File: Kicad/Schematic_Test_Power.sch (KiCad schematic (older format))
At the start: 17 parts, among them J201 USB_B_Micro, J202 Conn_02x01 BATTERY, SW201 SW_DIP_x01, U201 STBC08, U202 AP22811BW5, U203 TLV75528PDBV

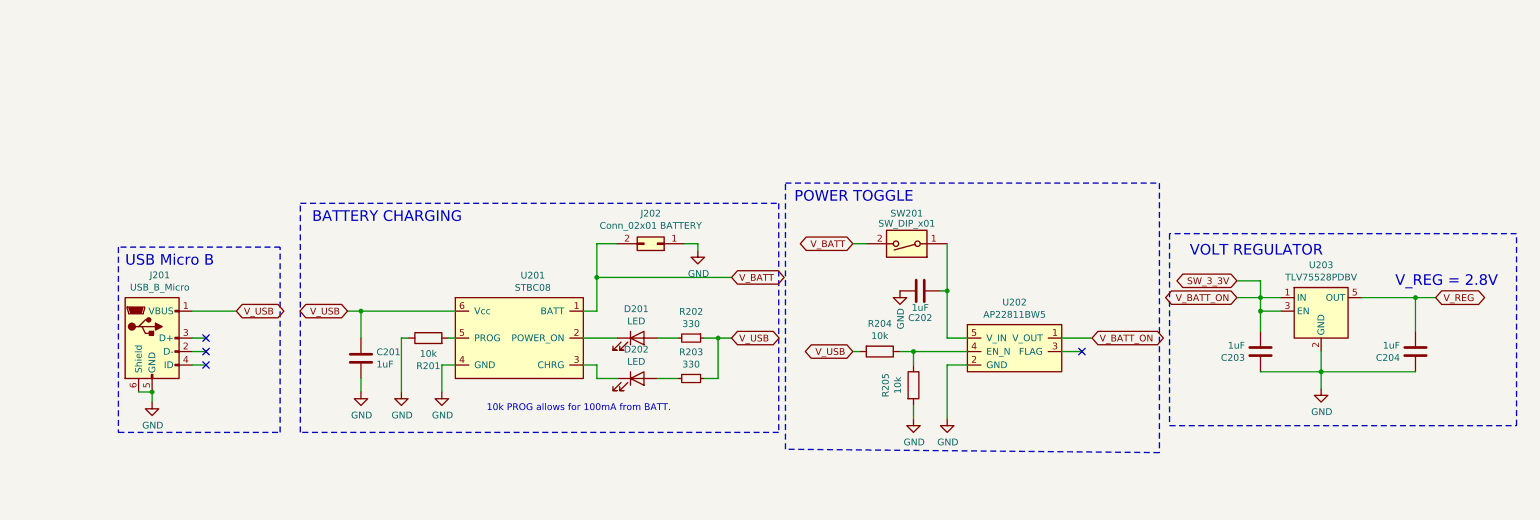
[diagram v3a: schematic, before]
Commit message: Calculating ram needed and current selected chip will not fit it.  Upgrading to a more capable chip.
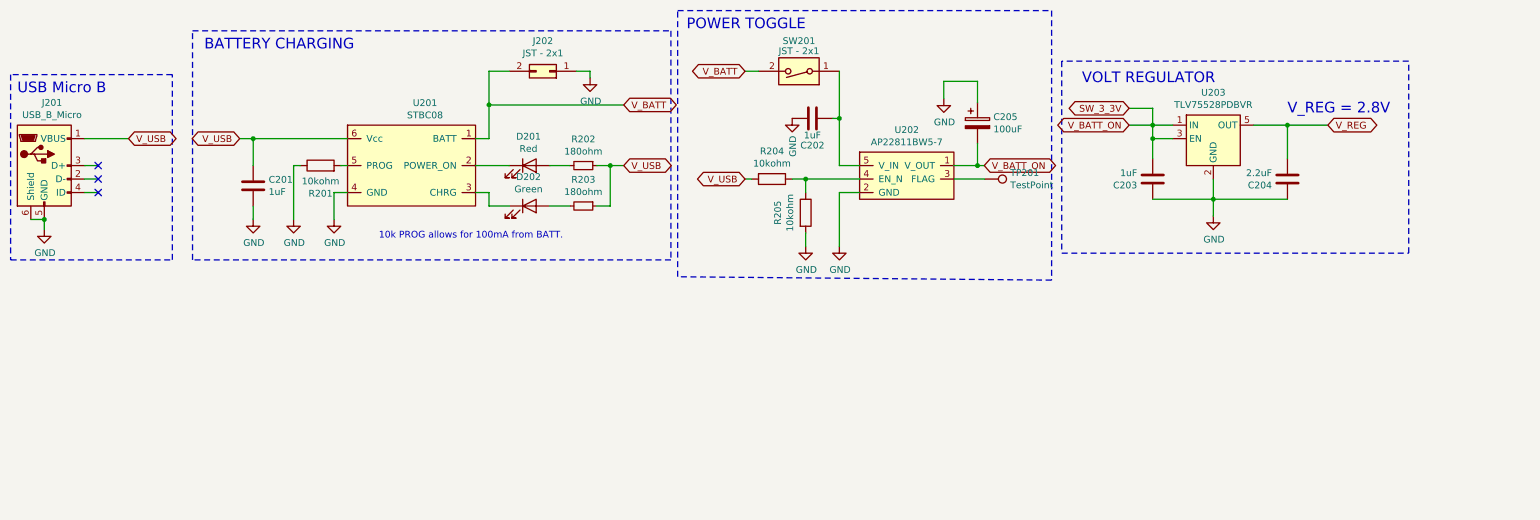
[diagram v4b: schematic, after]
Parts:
- added C205: 100uF, Capacitor_SMD:CP_Elec_6.3x5.2, symbol Device:CP
- added TP201: TestPoint, TestPoint:TestPoint_Pad_D1.0mm, symbol Connector:TestPoint
- C204: value 1uF -> 2.2uF; part_url https://www.digikey.com/product-detail/en/w%C3%BCrth-elektronik/885012107015/732-7625-1-ND/5454252 -> https://www.digikey.com/product-detail/en/w%C3%BCrth-elektronik/885012107001/732-7612-1-ND/5454239
- D201: value LED -> Red; part_details RED when ERROR -> Red when charging error
- D202: value LED -> Green; part_details GREEN when CHARGING -> Green when charging
- J202: value Conn_02x01 BATTERY -> JST - 2x1; part_details JST - 2 pin -> (none); part_name (none) -> Battery Connector; part_url LOCAL STOCK -> (none)
- R201, R204, R205: value 10k -> 10kohm
- R202, R203: value 330 -> 180ohm; part_url https://www.digikey.com/product-detail/en/yageo/RC1206FR-07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 -> https://www.digikey.com/product-detail/en/stackpole-electro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
- SW201: value SW_DIP_x01 -> JST - 2x1; part_details JST - 2 pin (switch attached to case) -> Power toggle
- U201: part_details Lithium Ion Battery Recharge IC -> (none); part_name STBC08PMR -> Lithium Ion Battery Charging IC
- U202: value AP22811BW5 -> AP22811BW5-7; part_details Mosfet, active low (batt protection) -> Battery protection switch; part_name AP22811BW5-7 -> Mosfet, active low
- U203: value TLV75528PDBV -> TLV75528PDBVR; part_details Linear Regulator, 2.8v 500mA, 230mV~ dropout -> 2.8v 500mA, 230mV~ dropout; part_name TLV75528PDBVR -> Linear Regulator
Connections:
- net GND: now also C205.1
- net SW_3_3V: now also C205.2
- net at U202.3 (FLAG): now also TP201.1
- no-connect marks 4 -> 3
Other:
- moved on the sheet: C201, C202, C203, D201, D202, J201, J202, R201, R202, R203, R204, R205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

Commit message: PCB updated to curved traces.  Leftover final polish, screw locations, drill-routing, and art is missing
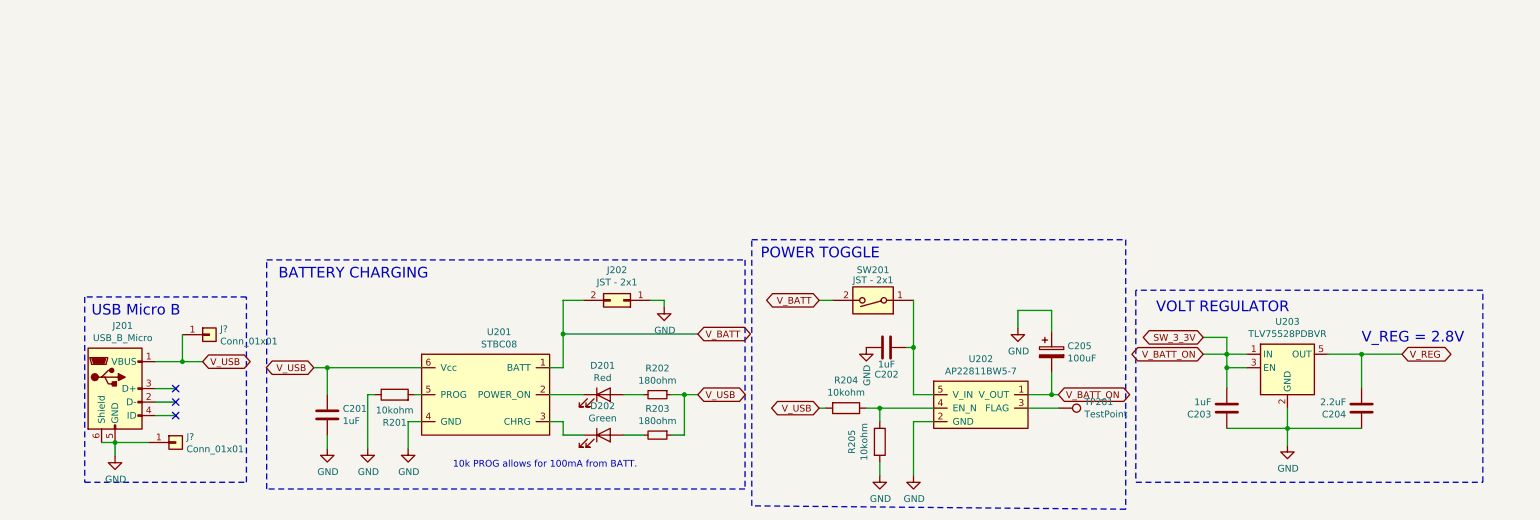
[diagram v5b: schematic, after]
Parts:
- added J? (x2): Conn_01x01, Connector_PinHeader_2.00mm:PinHeader_1x01_P2.00mm_Vertical, symbol Connector_Generic:Conn_01x01
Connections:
- net GND: now also J?.1 (Pin_1)
- net V_USB: now also J?.1 (Pin_1)
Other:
- moved on the sheet: C201, C202, C203, C204, C205, D201, D202, J201, J202, R201, R202, R203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

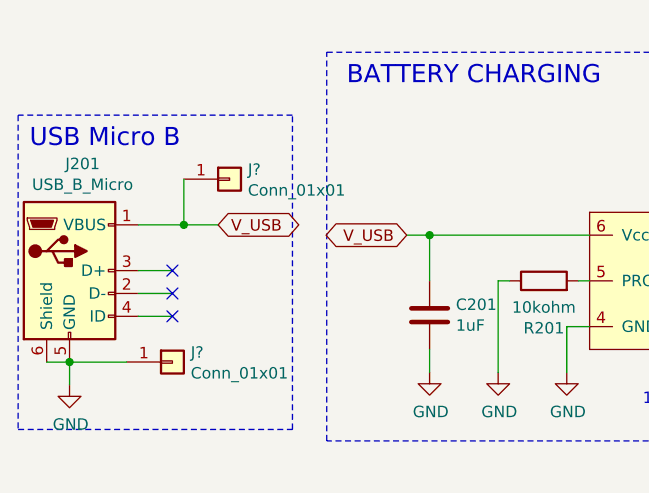
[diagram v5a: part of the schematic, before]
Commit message: Continued work on PCB.  Added back art.
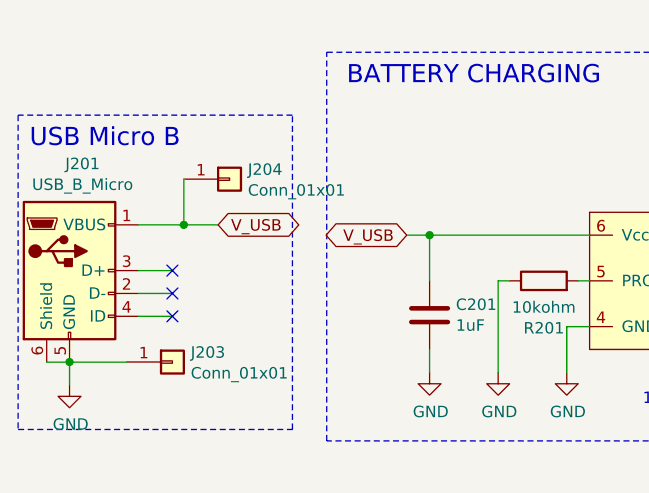
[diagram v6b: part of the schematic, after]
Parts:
- gave numbers to parts that had none: 2
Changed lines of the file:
@@
 	1050 4050 1250 4050
 $Comp
-L Connector_Generic:Conn_01x01 J?
+L Connector_Generic:Conn_01x01 J204
 U 1 1 5F8F328D
 P 1450 3850
-F 0 "J?" H 1530 3892 50  0000 L CNN
+F 0 "J204" H 1530 3892 50  0000 L CNN
 F 1 "Conn_01x01" H 1530 3801 50  0000 L CNN
 F 2 "Connector_PinHeader_2.00mm:PinHeader_1x01_P2.00mm_Vertical" H 1450 3850 50  0001 C CNN
@@
 $EndComp
 $Comp
-L Connector_Generic:Conn_01x01 J?
+L Connector_Generic:Conn_01x01 J203
 U 1 1 5F8F4320
 P 1200 4650
-F 0 "J?" H 1280 4692 50  0000 L CNN
+F 0 "J203" H 1280 4692 50  0000 L CNN
 F 1 "Conn_01x01" H 1280 4601 50  0000 L CNN
 F 2 "Connector_PinHeader_2.00mm:PinHeader_1x01_P2.00mm_Vertical" H 1200 4650 50  0001 C CNN

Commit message: Purchases made, case ordered, PCB ordered, parts ordered, money not happy.
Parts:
- C201, C202, C203: PURCHASED (none) -> 12x
- C204, D201, D202: PURCHASED (none) -> 6x
- C205, J201, U201, U202, U203: PURCHASED (none) -> 3x
- J202, J203, J204, TP201: PURCHASED (none) -> x
- R201, R204, R205: PURCHASED (none) -> 24x
- R202, R203: PURCHASED (none) -> 9x
- SW201: PURCHASED (none) -> 10x
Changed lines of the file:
@@
 F 4 "Capactitor - Bypass" H 7700 3980 50  0001 C CNN "part_name"
 F 5 "https://www.digikey.com/product-detail/en/w%C3%BCrth-elektronik/865230143004/732-8282-1-ND/5728239" H 7700 3980 50  0001 C CNN "part_url"
+F 6 "3x" H 7700 3980 50  0001 C CNN "PURCHASED"
 	1    7700 3980
 	1    0    0    -1
@@
 F 5 "Linear Regulator" H 9450 4095 50  0001 C CNN "part_name"
 F 6 "https://www.digikey.com/product-detail/en/texas-instruments/TLV75528PDBVR/296-51798-1-ND/9746161" H 9450 4095 50  0001 C CNN "part_url"
+F 7 "3x" H 9450 4095 50  0001 C CNN "PURCHASED"
 	1    9450 4095
 	1    0    0    -1
@@
 F 3 "~" H 7955 4395 50  0001 C CNN
 F 4 "Test point for U202 error (low imp. on error)" H 7755 4395 50  0001 C CNN "part_details"
+F 5 "x" H 7755 4395 50  0001 C CNN "PURCHASED"
 	1    7755 4395
 	0    1    1    0
@@
 F 5 "Lithium Ion Battery Charging IC" H 3475 3945 50  0001 C CNN "part_name"
 F 6 "https://www.digikey.com/product-detail/en/stmicroelectronics/STBC08PMR/497-5808-6-ND/1506505" H 3475 3945 50  0001 C CNN "part_url"
+F 7 "3x" H 3475 3945 50  0001 C CNN "PURCHASED"
 	1    3475 3945
 	1    0    0    -1
@@
 F 4 "Resistor - LED Status" H 4775 4295 50  0001 C CNN "part_name"
 F 5 "https://www.digikey.com/product-detail/en/stackpole-electronics-inc/RNCP1206FTD180R/RNCP1206FTD180RCT-ND/2240658" H 4775 4295 50  0001 C CNN "part_url"
+F 6 "9x" H 4775 4295 50  0001 C CNN "PURCHASED"
 	1    4775 4295
 	0    1    1    0
@@
 F 4 "Resistor - LED Status" H 4775 4595 50  0001 C CNN "part_name"
 F 5 "https://www.digikey.com/product-detail/en/stackpole-electronics-inc/RNCP1206FTD180R/RNCP1206FTD180RCT-ND/2240658" H 4775 4595 50  0001 C CNN "part_url"
+F 6 "9x" H 4775 4595 50  0001 C CNN "PURCHASED"
 	1    4775 4595
 	0    1    1    0
@@
 F 5 "https://www.digikey.com/product-detail/en/w%C3%BCrth-elektronik/156120RS75000/732-5030-1-ND/4490054" H 4375 4295 50  0001 C CNN "part_url"
 F 6 "LED - Red" H 4375 4295 50  0001 C CNN "part_name"
+F 7 "6x" H 4375 4295 50  0001 C CNN "PURCHASED"
 	1    4375 4295
 	1    0    0    -1
@@
 F 5 "LED - Green" H 4375 4595 50  0001 C CNN "part_name"
 F 6 "https://www.digikey.com/product-detail/en/w%C3%BCrth-elektronik/156120VS75000/732-5032-1-ND/4490060" H 4375 4595 50  0001 C CNN "part_url"
+F 7 "6x" H 4375 4595 50  0001 C CNN "PURCHASED"
 	1    4375 4595
 	1    0    0    -1
@@
 F 5 "Resistor - Prog" H 2825 4295 50  0001 C CNN "part_name"
 F 6 "https://www.digikey.com/product-detail/en/yageo/RC1206JR-0710KL/311-10KERCT-ND/732156" H 2825 4295 50  0001 C CNN "part_url"
+F 7 "24x" H 2825 4295 50  0001 C CNN "PURCHASED"
 	1    2825 4295
 	0    -1   -1   0
@@
 F 4 "Capactitor - Bypass" H 2325 4445 50  0001 C CNN "part_name"
 F 5 "https://www.digikey.com/product-detail/en/w%C3%BCrth-elektronik/885012107015/732-7625-1-ND/5454252" H 2325 4445 50  0001 C CNN "part_url"
+F 6 "12x" H 2325 4445 50  0001 C CNN "PURCHASED"
 	1    2325 4445
 	1    0    0    -1
@@
 F 5 "" H 4525 3595 50  0001 C CNN "part_url"
 F 6 "Battery Connector" H 4525 3595 50  0001 C CNN "part_name"
+F 7 "x" H 4525 3595 50  0001 C CNN "PURCHASED"
 	1    4525 3595
 	-1   0    0    1
@@
 F 5 "Mosfet, active low" H 7175 4195 50  0001 C CNN "part_name"
 F 6 "https://www.digikey.com/product-detail/en/diodes-incorporated/AP22811BW5-7/AP22811BW5-7DICT-ND/8545787" H 7175 4195 50  0001 C CNN "part_url"
+F 7 "3x" H 7175 4195 50  0001 C CNN "PURCHASED"
 	1    7175 4195
 	1    0    0    -1
@@
 F 4 "Capactitor - Bypass" H 6475 3945 50  0001 C CNN "part_name"
 F 5 "https://www.digikey.com/product-detail/en/w%C3%BCrth-elektronik/885012107015/732-7625-1-ND/5454252" H 6475 3945 50  0001 C CNN "part_url"
+F 6 "12x" H 6475 3945 50  0001 C CNN "PURCHASED"
 	1    6475 3945
 	0    1    1    0
@@
 F 6 "Resistor - Pull Up" H 6425 4645 50  0001 C CNN "part_name"
 F 7 "https://www.digikey.com/product-detail/en/yageo/RC1206JR-0710KL/311-10KERCT-ND/732156" H 6425 4645 50  0001 C CNN "part_url"
+F 8 "24x" H 6425 4645 50  0001 C CNN "PURCHASED"
 	1    6425 4645
 	1    0    0    -1
@@
 F 6 "Resistor - Pull Up" H 6175 4395 50  0001 C CNN "part_name"
 F 7 "https://www.digikey.com/product-detail/en/yageo/RC1206JR-0710KL/311-10KERCT-ND/732156" H 6175 4395 50  0001 C CNN "part_url"
+F 8 "24x" H 6175 4395 50  0001 C CNN "PURCHASED"
 	1    6175 4395
 	0    1    1    0
@@
 F 5 "Switch - Power" H 6375 3595 50  0001 C CNN "part_name"
 F 6 "https://www.amazon.com/MTS-101-Position-Miniature-Toggle-Switch/dp/B0799LBFNY/ref=lp_306596011_1_8?s=industrial&ie=UTF8&qid=1599516393&sr=1-8" H 6375 3595 50  0001 C CNN "part_url"
+F 7 "10x" H 6375 3595 50  0001 C CNN "PURCHASED"
 	1    6375 3595
 	-1   0    0    1
@@
 F 4 "Capactitor - Bypass" H 9000 4395 50  0001 C CNN "part_name"
 F 5 "https://www.digikey.com/product-detail/en/w%C3%BCrth-elektronik/885012107015/732-7625-1-ND/5454252" H 9000 4395 50  0001 C CNN "part_url"
+F 6 "12x" H 9000 4395 50  0001 C CNN "PURCHASED"
 	1    9000 4395
 	-1   0    0    1
@@
 F 4 "https://www.digikey.com/product-detail/en/w%C3%BCrth-elektronik/885012107001/732-7612-1-ND/5454239" H 10000 4395 50  0001 C CNN "part_url"
 F 5 "Capactitor - Bypass" H 10000 4395 50  0001 C CNN "part_name"
+F 6 "6x" H 10000 4395 50  0001 C CNN "PURCHASED"
 	1    10000 4395
 	-1   0    0    1
@@
 F 5 "Only used for charging" H 750 4250 50  0001 C CNN "part_details"
 F 6 "https://www.digikey.com/product-detail/en/amphenol-icc-fci/10103594-0001LF/609-4050-1-ND/2350357" H 750 4250 50  0001 C CNN "part_url"
+F 7 "3x" H 750 4250 50  0001 C CNN "PURCHASED"
 	1    750  4250
 	1    0    0    -1
@@
 F 3 "~" H 1450 3850 50  0001 C CNN
 F 4 "DO_NOT_SHOW" H 1450 3850 50  0001 C CNN "part_details"
+F 5 "x" H 1450 3850 50  0001 C CNN "PURCHASED"
 	1    1450 3850
 	1    0    0    -1
@@
 F 3 "~" H 1200 4650 50  0001 C CNN
 F 4 "DO_NOT_SHOW" H 1200 4650 50  0001 C CNN "part_details"
+F 5 "x" H 1200 4650 50  0001 C CNN "PURCHASED"
 	1    1200 4650
 	1    0    0    -1

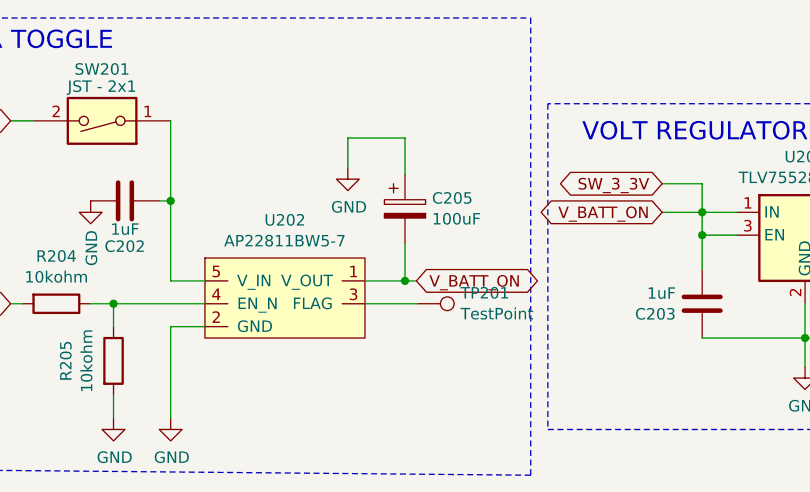
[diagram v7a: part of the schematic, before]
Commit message: Added images.  Small schematic corrections
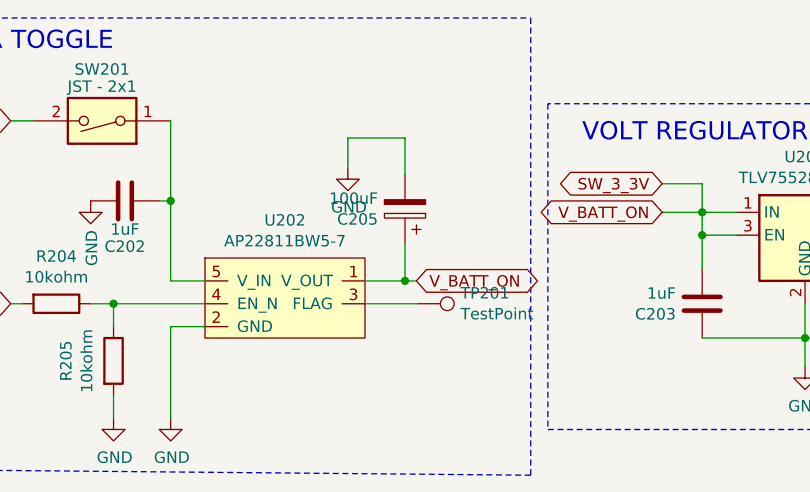
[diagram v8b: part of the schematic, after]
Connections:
- net GND: now also C205.2; no longer C205.1
- net SW_3_3V: now also C205.1; no longer C205.2
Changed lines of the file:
@@
 F 6 "3x" H 7700 3980 50  0001 C CNN "PURCHASED"
 	1    7700 3980
-	1    0    0    -1
+	-1   0    0    1
 $EndComp
 $Comp
